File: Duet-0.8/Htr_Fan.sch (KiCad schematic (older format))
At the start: 38 parts, among them J27 TP

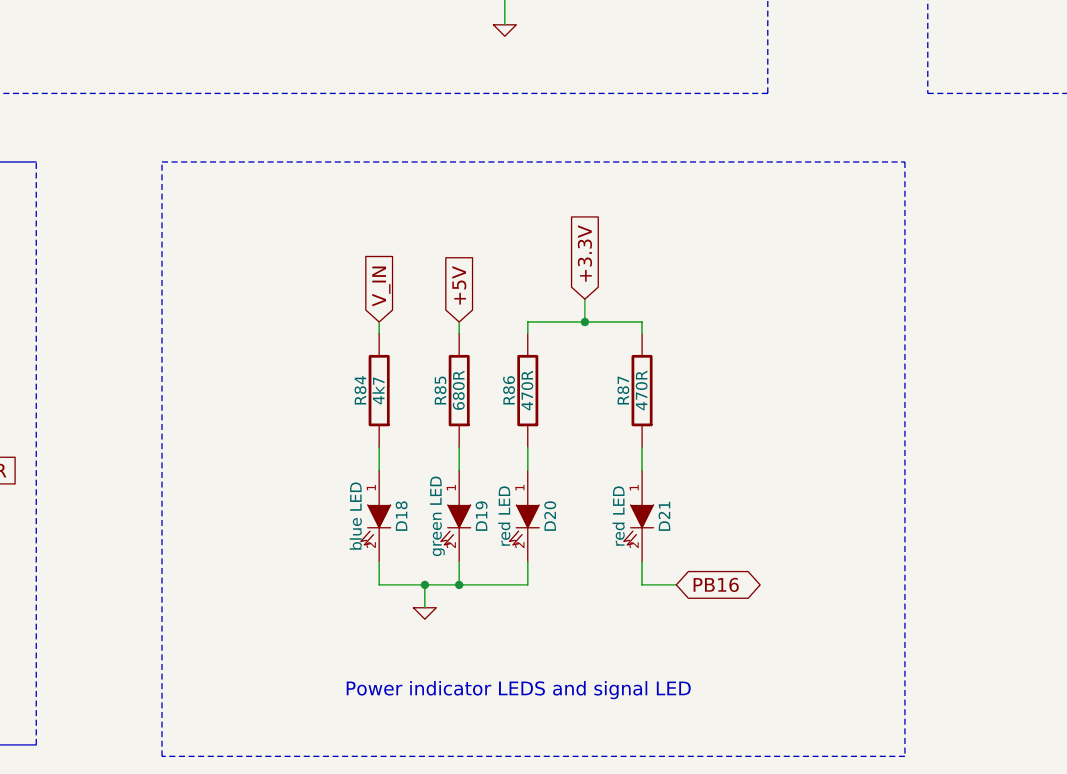
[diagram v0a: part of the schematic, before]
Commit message: Duet Version 0.8 ----------------
Schematic changed; board still needs to be updated.

Changes:

Probe rewired to use AD12 and AD14, (standard P2 probe in the Firmware)
Bed connector - both spades and screw terminals used
Power connector - both spades and screw terminals used
Spurious power LEDS removed - there is now only one set
5V connector removed.  PS on is now a single pin.
Second Z connector added in series with the first.
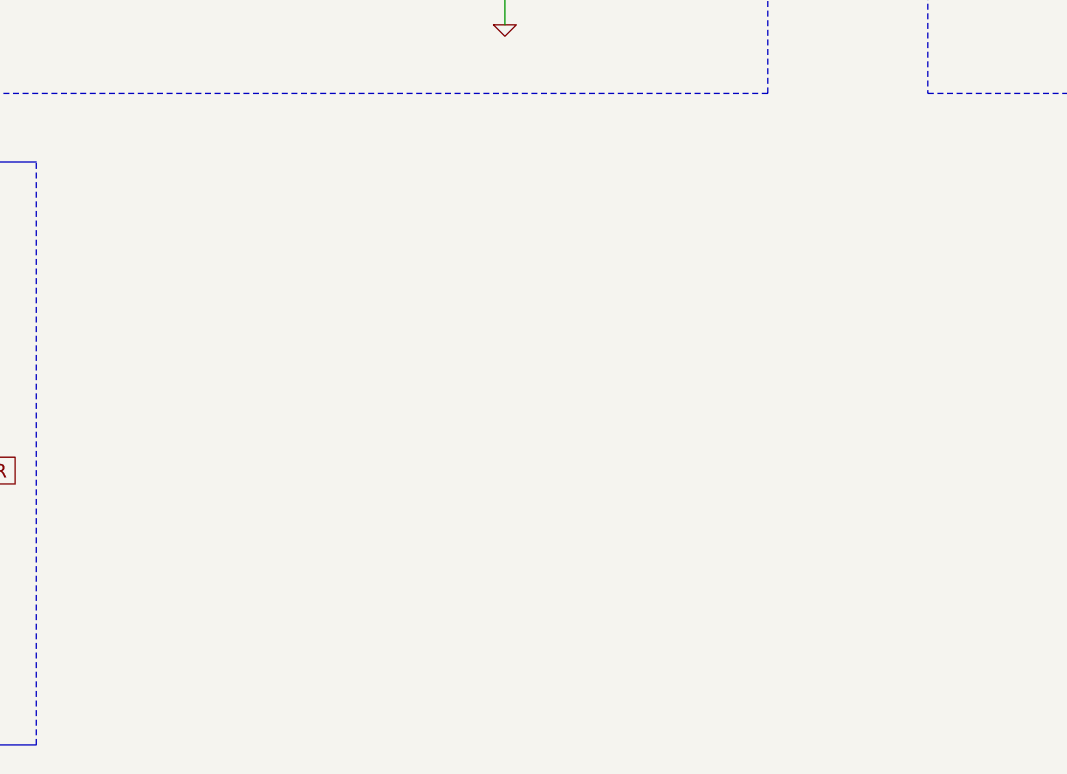
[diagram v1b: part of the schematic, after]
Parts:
- removed D18: blue LED, symbol LED
- removed D19: green LED, symbol LED
- removed D20, D21: red LED, symbol LED
- removed R84: 4k7, symbol R
- removed R85: 680R, symbol R
- removed R86, R87: 470R, symbol R
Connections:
- net labels removed: PB16
- wire segments 104 -> 87
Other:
- note removed: "Power indicator LEDS and signal LED"
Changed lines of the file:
@@
 LIBS:valves
 LIBS:FE
-LIBS:Duet0.7-cache
+LIBS:Shield-cache
+LIBS:Duet0.8-cache
 EELAYER 27 0
 EELAYER END
@@
 Sheet 6 7
 Title "Duet"
-Date "16 jan 2015"
+Date "27 feb 2015"
 Rev "0.7"
 Comp "Think3DPrint3D, RepRapPro"
@@
 FAN0-
 $Comp
-L GND #PWR054
+L GND #PWR053
 U 1 1 5090541F
 P 11600 4450
-F 0 "#PWR054" H 11600 4450 30  0001 C CNN
+F 0 "#PWR053" H 11600 4450 30  0001 C CNN
 F 1 "GND" H 11600 4380 30  0001 C CNN
 F 2 "" H 11600 4450 60  0001 C CNN
@@
 $EndComp
 $Comp
-L GND #PWR055
+L GND #PWR054
 U 1 1 50905416
 P 7400 4450
-F 0 "#PWR055" H 7400 4450 30  0001 C CNN
+F 0 "#PWR054" H 7400 4450 30  0001 C CNN
 F 1 "GND" H 7400 4380 30  0001 C CNN
 F 2 "" H 7400 4450 60  0001 C CNN
@@
 BED-
 $Comp
-L GND #PWR056
+L GND #PWR055
 U 1 1 5064BB75
 P 3300 4450
-F 0 "#PWR056" H 3300 4450 30  0001 C CNN
+F 0 "#PWR055" H 3300 4450 30  0001 C CNN
 F 1 "GND" H 3300 4380 30  0001 C CNN
 F 2 "" H 3300 4450 60  0001 C CNN
@@
 Text GLabel 2250 1800 1    60   Input ~ 0
 +5V
-Wire Wire Line
-	6850 6300 6850 6400
-Wire Wire Line
-	6850 5800 6850 5750
-Wire Wire Line
-	6850 6800 6850 6900
-$Comp
-L LED D18
-U 1 1 5491B59F
-P 6850 6600
-F 0 "D18" H 6850 6700 50  0000 C CNN
-F 1 "blue LED" H 6850 6500 50  0000 C CNN
-F 2 "" H 6850 6600 60  0001 C CNN
-F 3 "" H 6850 6600 60  0001 C CNN
-	1    6850 6600
-	0    1    1    0
-$EndComp
-$Comp
-L R R84
-U 1 1 5491B5A5
-P 6850 6050
-F 0 "R84" V 6930 6050 50  0000 C CNN
-F 1 "4k7" V 6850 6050 50  0000 C CNN
-F 2 "" H 6850 6050 60  0001 C CNN
-F 3 "" H 6850 6050 60  0001 C CNN
-	1    6850 6050
-	-1   0    0    1
-$EndComp
-Wire Wire Line
-	7200 6300 7200 6400
-Wire Wire Line
-	7200 5800 7200 5750
-Wire Wire Line
-	7200 6800 7200 6900
-$Comp
-L LED D19
-U 1 1 5491B5BB
-P 7200 6600
-F 0 "D19" H 7200 6700 50  0000 C CNN
-F 1 "green LED" H 7200 6500 50  0000 C CNN
-F 2 "" H 7200 6600 60  0001 C CNN
-F 3 "" H 7200 6600 60  0001 C CNN
-	1    7200 6600
-	0    1    1    0
-$EndComp
-$Comp
-L R R85
-U 1 1 5491B5C1
-P 7200 6050
-F 0 "R85" V 7280 6050 50  0000 C CNN
-F 1 "680R" V 7200 6050 50  0000 C CNN
-F 2 "" H 7200 6050 60  0001 C CNN
-F 3 "" H 7200 6050 60  0001 C CNN
-	1    7200 6050
-	-1   0    0    1
-$EndComp
-Wire Wire Line
-	7500 6300 7500 6400
-Wire Wire Line
-	7500 5800 7500 5750
-Wire Wire Line
-	7500 6900 7500 6800
-$Comp
-L LED D20
-U 1 1 5491B5CA
-P 7500 6600
-F 0 "D20" H 7500 6700 50  0000 C CNN
-F 1 "red LED" H 7500 6500 50  0000 C CNN
-F 2 "" H 7500 6600 60  0001 C CNN
-F 3 "" H 7500 6600 60  0001 C CNN
-	1    7500 6600
-	0    1    1    0
-$EndComp
-$Comp
-L R R86
-U 1 1 5491B5D0
-P 7500 6050
-F 0 "R86" V 7580 6050 50  0000 C CNN
-F 1 "470R" V 7500 6050 50  0000 C CNN
-F 2 "" H 7500 6050 60  0001 C CNN
-F 3 "" H 7500 6050 60  0001 C CNN
-	1    7500 6050
-	-1   0    0    1
-$EndComp
-Wire Wire Line
-	8000 6300 8000 6400
-Wire Wire Line
-	8000 5800 8000 5750
-Wire Wire Line
-	8000 6800 8000 6900
-$Comp
-L LED D21
-U 1 1 5491B5D9
-P 8000 6600
-F 0 "D21" H 8000 6700 50  0000 C CNN
-F 1 "red LED" H 8000 6500 50  0000 C CNN
-F 2 "" H 8000 6600 60  0001 C CNN
-F 3 "" H 8000 6600 60  0001 C CNN
-	1    8000 6600
-	0    1    1    0
-$EndComp
-$Comp
-L R R87
-U 1 1 5491B5DF
-P 8000 6050
-F 0 "R87" V 8080 6050 50  0000 C CNN
-F 1 "470R" V 8000 6050 50  0000 C CNN
-F 2 "" H 8000 6050 60  0001 C CNN
-F 3 "" H 8000 6050 60  0001 C CNN
-	1    8000 6050
-	-1   0    0    1
-$EndComp
-Wire Wire Line
-	6850 6900 7500 6900
-Connection ~ 7200 6900
-Wire Wire Line
-	7050 6900 7050 7000
-Connection ~ 7050 6900
-Wire Wire Line
-	8000 5750 7500 5750
-Wire Wire Line
-	7750 5750 7750 5650
-Connection ~ 7750 5750
-Text GLabel 6850 5750 1    60   Input ~ 0
-V_IN
-Text GLabel 7200 5750 1    60   Input ~ 0
-+5V
-Text GLabel 7750 5650 1    60   Input ~ 0
-+3.3V
-$Comp
-L GND #PWR057
-U 1 1 5491B8B7
-P 7050 7000
-F 0 "#PWR057" H 7050 7000 30  0001 C CNN
-F 1 "GND" H 7050 6930 30  0001 C CNN
-F 2 "" H 7050 7000 60  0001 C CNN
-F 3 "" H 7050 7000 60  0001 C CNN
-	1    7050 7000
-	1    0    0    -1
-$EndComp
-Text GLabel 8150 6900 2    60   BiDi ~ 0
-PB16
-Wire Wire Line
-	8000 6900 8150 6900
-Wire Notes Line
-	5900 5050 9150 5050
-Wire Notes Line
-	9150 5050 9150 7650
-Wire Notes Line
-	9150 7650 5900 7650
-Wire Notes Line
-	5900 7650 5900 5050
-Text Notes 6700 7400 0    60   ~ 0
-Power indicator LEDS and signal LED
 $EndSCHEMATC
